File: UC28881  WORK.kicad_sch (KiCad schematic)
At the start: 0 parts

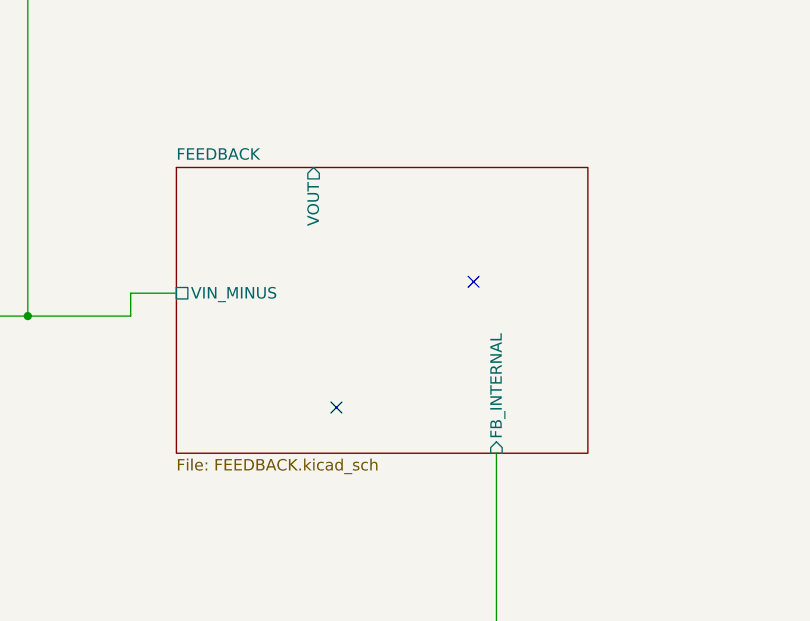
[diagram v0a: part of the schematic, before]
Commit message: Updated schematic and fixed silkscreen overlap
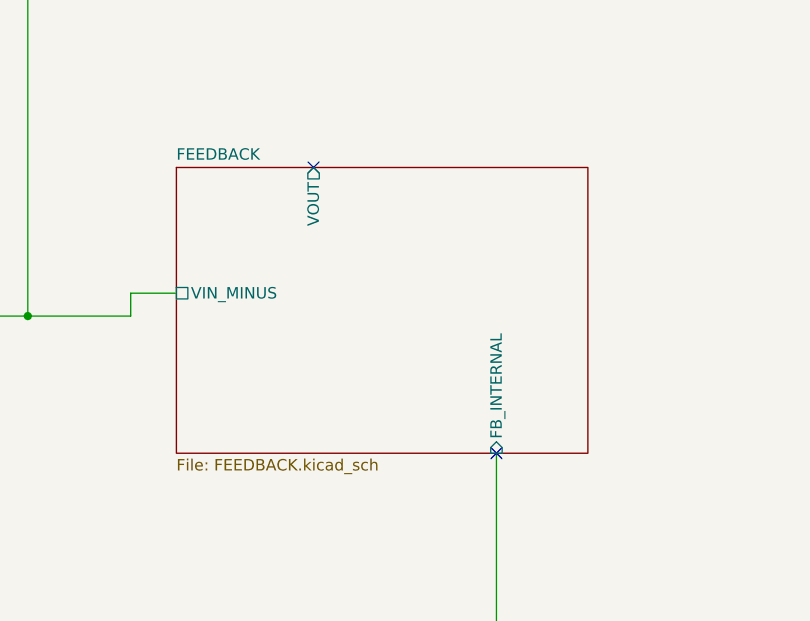
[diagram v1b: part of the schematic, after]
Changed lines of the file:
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@@
   (junction (at 146.05 93.98) (diameter 0) (color 0 0 0 0)
   )
-  (no_connect (at 180.34 104.14))
-  (no_connect (at 195.58 90.17))
+  (no_connect (at 177.8 77.47))
+  (no_connect (at 198.12 109.22))
   (wire (pts (xy 85.09 53.34) (xy 85.09 87.63))
     (stroke (width 0) (type default))

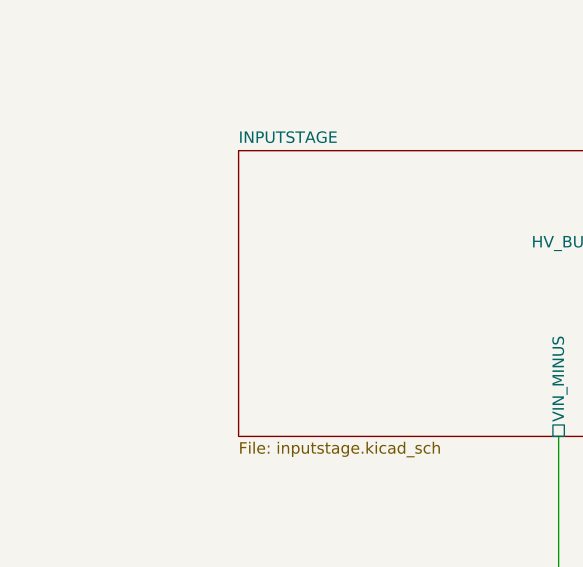
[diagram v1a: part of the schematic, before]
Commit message: Updated schematic and added RS485 protection circuit
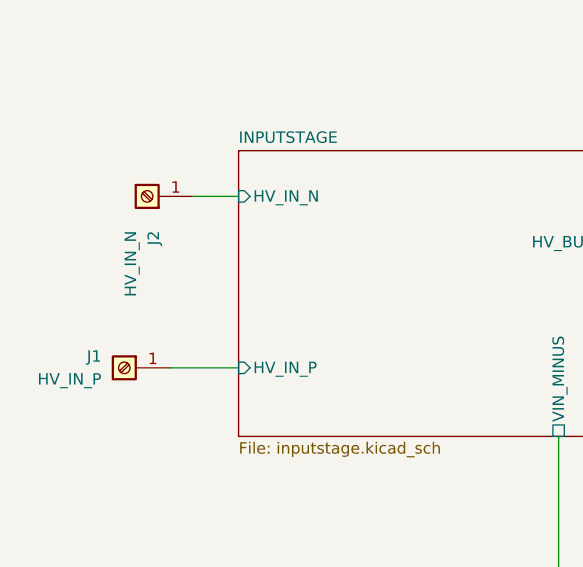
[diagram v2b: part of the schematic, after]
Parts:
- added J1: HV_IN_P, symbol Connector:Screw_Terminal_01x01
- added J2: HV_IN_N, symbol Connector:Screw_Terminal_01x01
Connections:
- new net INPUTSTAGE/HV_IN_N: J2.1 (Pin_1)
- new net INPUTSTAGE/HV_IN_P: J1.1 (Pin_1)
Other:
- sheet INPUTSTAGE ports: added HV_IN_N, HV_IN_P; removed none
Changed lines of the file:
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@@
+    (stroke (width 0) (type default))
+  )
+  (wire (pts (xy 22.86 67.31) (xy 30.48 67.31))
     (stroke (width 0) (type default))
   )
@@
   )
   (wire (pts (xy 111.76 43.18) (xy 111.76 27.94))
+    (stroke (width 0) (type default))
+  )
+  (wire (pts (xy 25.4 48.26) (xy 30.48 48.26))
     (stroke (width 0) (type default))
   )
@@
   (wire (pts (xy 66.04 93.98) (xy 146.05 93.98))
     (stroke (width 0) (type default))
+  )
+  (symbol (lib_id "Connector:Screw_Terminal_01x01") (at 20.32 48.26 180) (unit 1)
+    (in_bom yes) (on_board yes) (dnp no)
+    (property "Reference" "J2" (at 21.0439 52.07 90)
+      (effects (font (size 1.27 1.27)) (justify left))
+    )
+    (property "Value" "HV_IN_N" (at 18.5039 52.07 90)
+      (effects (font (size 1.27 1.27)) (justify left))
+    )
+    (property "Footprint" "" (at 20.32 48.26 0)
+      (effects (font (size 1.27 1.27)) hide)
+    )
+    (property "Datasheet" "~" (at 20.32 48.26 0)
+      (effects (font (size 1.27 1.27)) hide)
+    )
+    (pin "1")
+    (instances
+      (project "UC28881  WORK"
+        (path "/02261b3b-0ab5-411c-b90d-2981c1ef32c1"
+          (reference "J2") (unit 1)
+        )
+      )
+    )
+  )
+  (symbol (lib_id "Connector:Screw_Terminal_01x01") (at 17.78 67.31 0) (mirror y) (unit 1)
+    (in_bom yes) (on_board yes) (dnp no)
+    (property "Reference" "J1" (at 15.24 66.04 0)
+      (effects (font (size 1.27 1.27)) (justify left))
+    )
+    (property "Value" "HV_IN_P" (at 15.24 68.58 0)
+      (effects (font (size 1.27 1.27)) (justify left))
+    )
+    (property "Footprint" "" (at 17.78 67.31 0)
+      (effects (font (size 1.27 1.27)) hide)
+    )
+    (property "Datasheet" "~" (at 17.78 67.31 0)
+      (effects (font (size 1.27 1.27)) hide)
+    )
+    (property "Sim.Enable" "0" (at 17.78 67.31 0)
+      (effects (font (size 1.27 1.27)) hide)
+    )
+    (pin "1")
+    (instances
+      (project "UC28881  WORK"
+        (path "/02261b3b-0ab5-411c-b90d-2981c1ef32c1"
+          (reference "J1") (unit 1)
+        )
+      )
+    )
   )
   (sheet (at 162.56 77.47) (size 45.72 31.75) (fields_autoplaced)
@@
       (effects (font (size 1.27 1.27)) (justify right))
     )
+    (pin "HV_IN_N" input (at 30.48 48.26 180)
+      (effects (font (size 1.27 1.27)) (justify left))
+    )
+    (pin "HV_IN_P" input (at 30.48 67.31 180)
+      (effects (font (size 1.27 1.27)) (justify left))
+    )
     (instances

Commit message: Updated KiCad project and schematic files
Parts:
- added C1: 10U, Capacitor_THT:CP_Radial_D12.5mm_P7.50mm, symbol Device:C_Polarized_Small
- added C2: 0.1u, Capacitor_THT:C_Rect_L18.0mm_W7.0mm_P15.00mm_FKS3_FKP3, symbol Device:C
- added C3: 100n, Capacitor_THT:C_Rect_L18.0mm_W7.0mm_P15.00mm_FKS3_FKP3, symbol Device:C
- added C4: 15n, Capacitor_THT:C_Rect_L18.0mm_W7.0mm_P15.00mm_FKS3_FKP3, symbol Device:C
- added CBULK1: 10U, Capacitor_THT:CP_Radial_D10.0mm_P5.00mm, symbol Device:C_Polarized_Small
- added CL1: 330u, 350uf:350UF CAP_14102E3_VIS, symbol Device:C_Polarized_Small
- added D1, D2: D, symbol Device:D
- added D3: 1N5819, Diode_THT:D_DO-41_SOD81_P10.16mm_Horizontal, symbol Diode:1N5819
- added F1: 0.1, 100nf:100NF CAPC1005X55N, symbol Device:Fuse
- added J3: 10V_OUT_P, symbol Connector:Screw_Terminal_01x01
- added J4: 10V_OUT_N, symbol Connector:Screw_Terminal_01x01
- added L1: 1, Inductor_SMD:L_7.3x7.3_H3.5, symbol Device:L
- added L2: 1M, Inductor_SMD:L_12x12mm_H8mm, symbol Device:L
- added RFB1: 10k, 10k resistor:RESC2012X65N, symbol Device:R
- added RFB2: 87.7K, 121k resistor:121K RES_ERJ8ENF1213V, symbol Device:R
- added Rf1: 10, Resistor_THT:R_Axial_DIN0922_L20.0mm_D9.0mm_P30.48mm_Horizontal, symbol Device:R
- added TVS1: D_Zener, symbol Device:D_Zener
- added U1: UCC28881, UCC2881:TI_SOIC-8_D_UCC28881_1.27mm, symbol New_Library for UCC28881:UCC28881
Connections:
- net INPUTSTAGE/HV_IN_N renamed Earth
- net Earth: now also C1.2, CBULK1.2, CL1.2, D1.2 (A), D3.2 (A), J4.1 (Pin_1), TVS1.2 (A)
- net INPUTSTAGE/HV_IN_P: no longer names the net of J1.1 (Pin_1)
- net INPUTSTAGE/HV_IN_P: now also Rf1.1
- new net: C1.1, L1.2, U1.5 (HVIN), U1.8 (DRAIN)
- new net: C2.2, C3.2, C4.2, D1.1 (K), L2.1, RFB1.1, U1.1 (GND), U1.2 (GND)
- new net: F1.1, Rf1.2
- new net: CBULK1.1, F1.2, L1.1, TVS1.1 (K)
- new net: CL1.1, D2.2 (A), D3.1 (K), J3.1 (Pin_1), L2.2
- new net: C4.1, D2.1 (K), RFB2.2
- new net: C2.1, U1.4 (VDD)
- new net Feedback pin: C3.1, RFB1.2, RFB2.1, U1.3 (FB)
- no-connect marks 2 -> 1
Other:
- removed sheet FEEDBACK
- removed sheet INPUTSTAGE
- removed sheet POWER
- moved on the sheet: J1
